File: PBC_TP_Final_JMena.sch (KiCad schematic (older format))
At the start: 0 parts

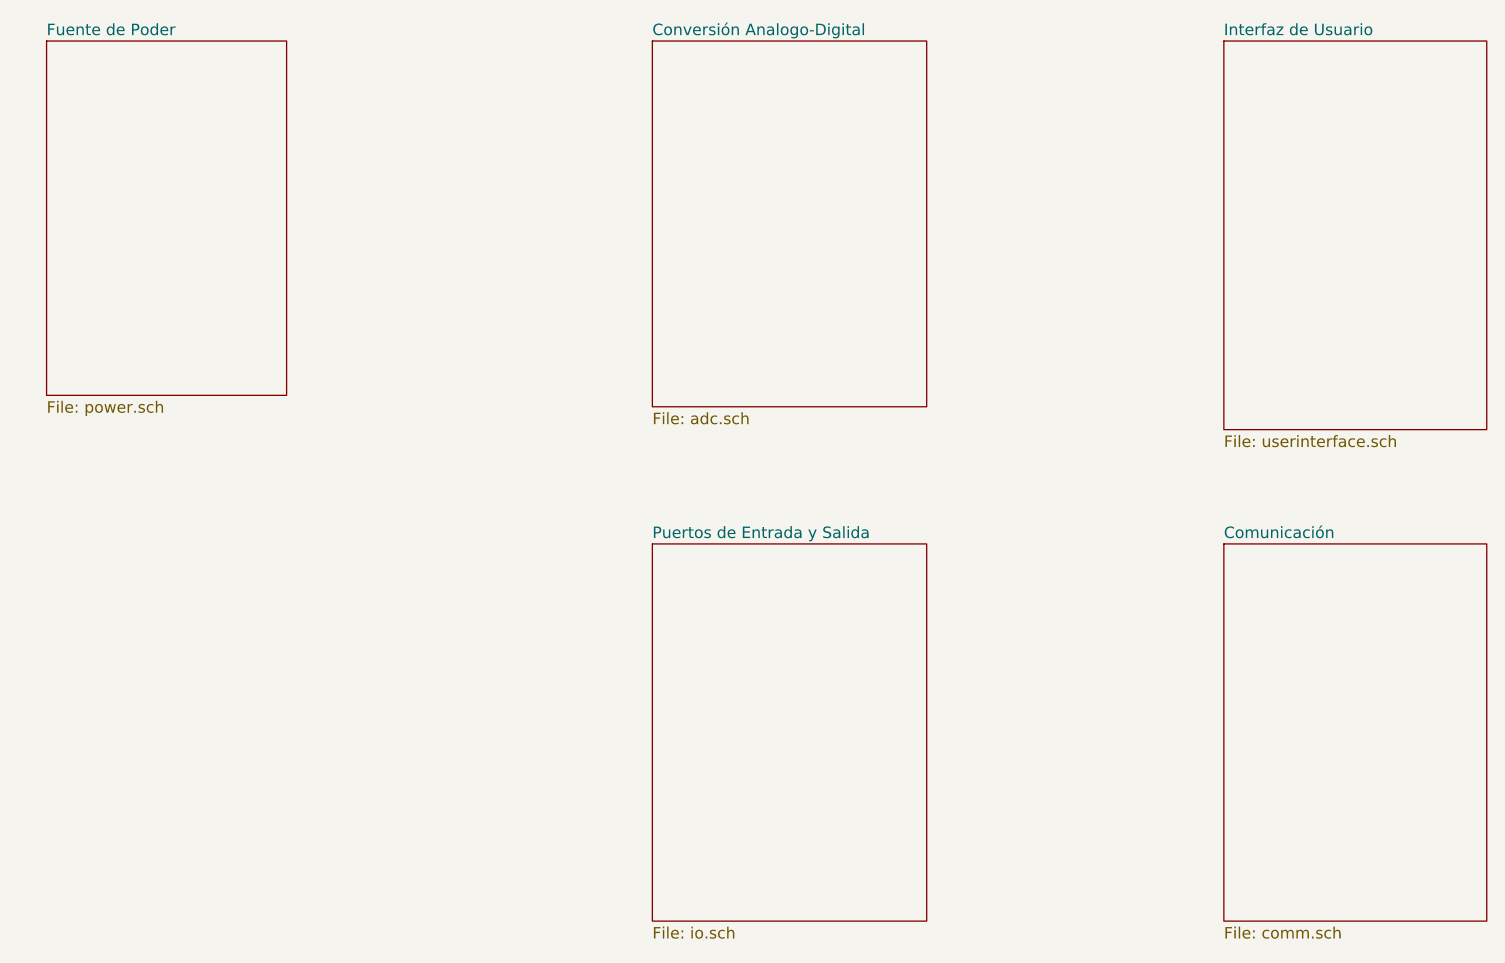
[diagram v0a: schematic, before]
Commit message: Se hace cambios en el esquematico y se anexa PCB
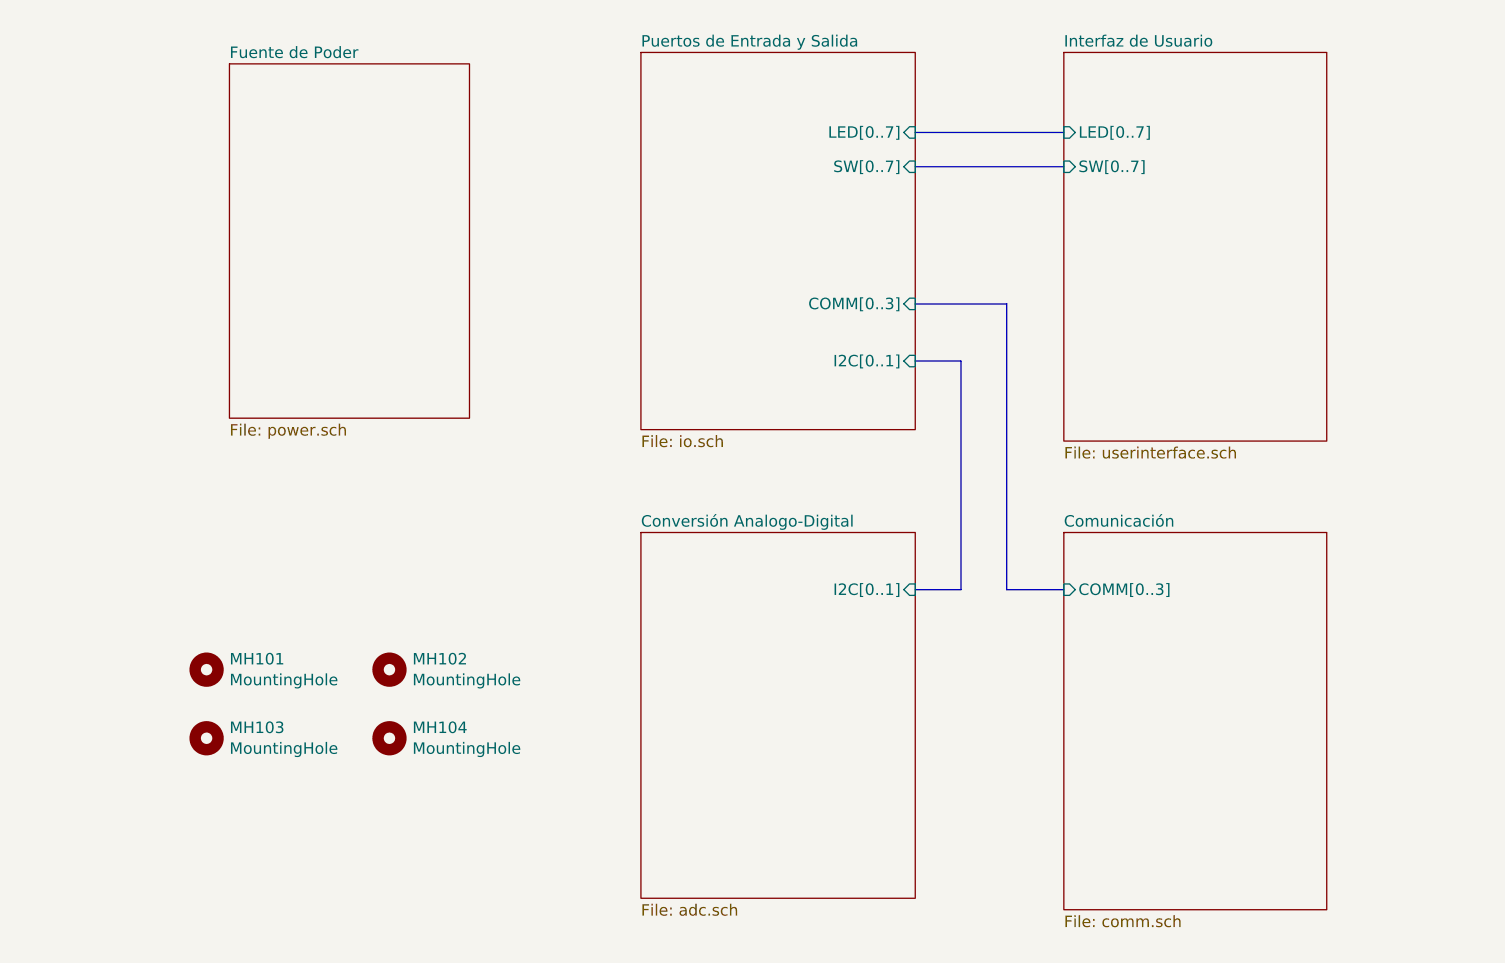
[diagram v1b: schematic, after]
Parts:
- added MH101, MH102, MH103, MH104: MountingHole, MountingHole:MountingHole_2.5mm, symbol Mechanical:MountingHole
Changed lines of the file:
@@
 $EndDescr
 $Sheet
-S 2750 1300 1050 1550
+S 3550 1400 1050 1550
 U 5BA8FAE3
 F0 "Fuente de Poder" 50
@@
 $EndSheet
 $Sheet
-S 5400 1300 1200 1600
+S 5350 3450 1200 1600
 U 5BA8FB15
 F0 "Conversión Analogo-Digital" 50
 F1 "adc.sch" 50
+F2 "I2C[0..1]" I R 6550 3700 50
 $EndSheet
+$Comp
+L Mechanical:MountingHole MH101
+U 1 1 5BB0B7F0
+P 3450 4050
+F 0 "MH101" H 3550 4096 50  0000 L CNN
+F 1 "MountingHole" H 3550 4005 50  0000 L CNN
+F 2 "MountingHole:MountingHole_2.5mm" H 3450 4050 50  0001 C CNN
+F 3 "~" H 3450 4050 50  0001 C CNN
+	1    3450 4050
+	1    0    0    -1
+$EndComp
+$Comp
+L Mechanical:MountingHole MH102
+U 1 1 5BB0B901
+P 4250 4050
+F 0 "MH102" H 4350 4096 50  0000 L CNN
+F 1 "MountingHole" H 4350 4005 50  0000 L CNN
+F 2 "MountingHole:MountingHole_2.5mm" H 4250 4050 50  0001 C CNN
+F 3 "~" H 4250 4050 50  0001 C CNN
+	1    4250 4050
+	1    0    0    -1
+$EndComp
+$Comp
+L Mechanical:MountingHole MH103
+U 1 1 5BB0B93D
+P 3450 4350
+F 0 "MH103" H 3550 4396 50  0000 L CNN
+F 1 "MountingHole" H 3550 4305 50  0000 L CNN
+F 2 "MountingHole:MountingHole_2.5mm" H 3450 4350 50  0001 C CNN
+F 3 "~" H 3450 4350 50  0001 C CNN
+	1    3450 4350
+	1    0    0    -1
+$EndComp
+$Comp
+L Mechanical:MountingHole MH104
+U 1 1 5BB0B985
+P 4250 4350
+F 0 "MH104" H 4350 4396 50  0000 L CNN
+F 1 "MountingHole" H 4350 4305 50  0000 L CNN
+F 2 "MountingHole:MountingHole_2.5mm" H 4250 4350 50  0001 C CNN
+F 3 "~" H 4250 4350 50  0001 C CNN
+	1    4250 4350
+	1    0    0    -1
+$EndComp
 $Sheet
-S 7900 1300 1150 1700
+S 7200 1350 1150 1700
 U 5BA8FB5C
 F0 "Interfaz de Usuario" 50
 F1 "userinterface.sch" 50
+F2 "LED[0..7]" I L 7200 1700 50
+F3 "SW[0..7]" I L 7200 1850 50
 $EndSheet
 $Sheet
-S 5400 3500 1200 1650
+S 5350 1350 1200 1650
 U 5BA8FCC3
 F0 "Puertos de Entrada y Salida" 50
 F1 "io.sch" 50
+F2 "LED[0..7]" I R 6550 1700 50
+F3 "SW[0..7]" I R 6550 1850 50
+F4 "COMM[0..3]" I R 6550 2450 50
+F5 "I2C[0..1]" I R 6550 2700 50
 $EndSheet
+Wire Bus Line
+	6550 1700 7200 1700
+Wire Bus Line
+	6550 1850 7200 1850
+Wire Bus Line
+	6550 2700 6750 2700
+Wire Bus Line
+	6750 2700 6750 3700
+Wire Bus Line
+	6750 3700 6550 3700
 $Sheet
-S 7900 3500 1150 1650
+S 7200 3450 1150 1650
 U 5BA8FCF6
 F0 "Comunicación" 50
 F1 "comm.sch" 50
+F2 "COMM[0..3]" I L 7200 3700 50
 $EndSheet
+Wire Bus Line
+	6950 2450 6550 2450
+Wire Bus Line
+	7200 3700 6950 3700
+Wire Bus Line
+	6950 3700 6950 2450
 $EndSCHEMATC

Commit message: Se realizan correcciones finales y se agregan carpetas BOM, Datasheet, Doc, Gerbers, lib.pretty y shapes3D
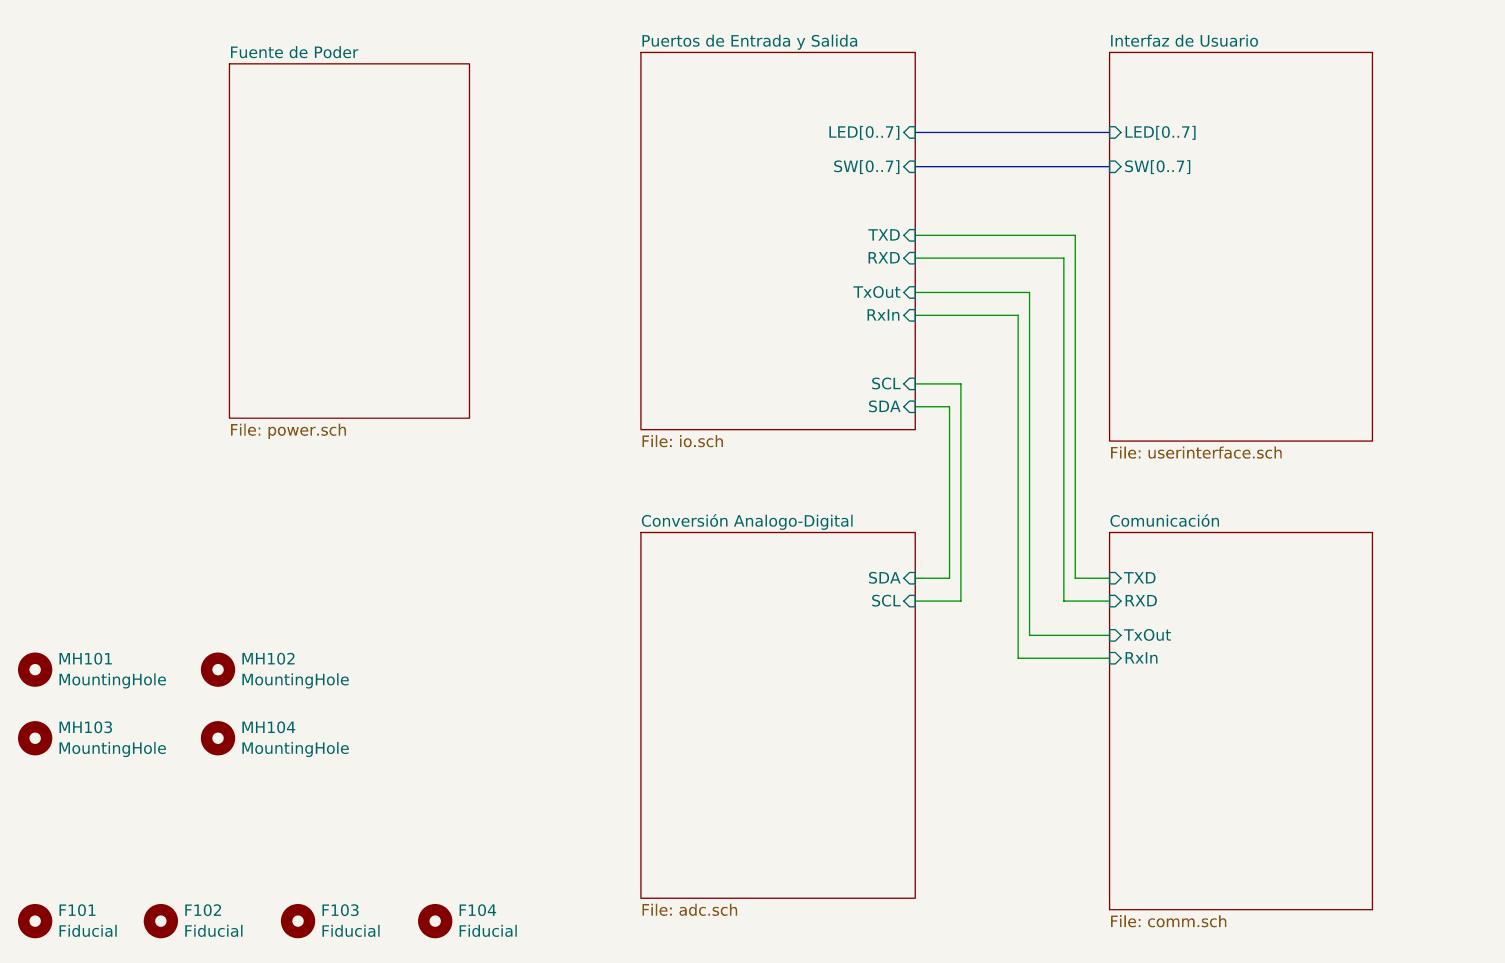
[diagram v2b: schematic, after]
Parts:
- added F101, F102, F103, F104: Fiducial, Fiducial:Fiducial_0.75mm_Dia_1.5mm_Outer, symbol Mechanical:MountingHole
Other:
- moved on the sheet: MH101, MH102, MH103, MH104
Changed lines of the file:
@@
 Sheet 1 6
 Title "PBC TP Final - Tarjeta de Expanción GEO-HCAL "
-Date "14/06/18"
+Date "2018-11-13"
 Rev "RG 1.0"
 Comp "GEO Technologies"
-Comment1 "Autor: Jairo Mena"
-Comment2 "Versión: 1.0"
-Comment3 ""
+Comment1 "Revisor: Telmo Moya"
+Comment2 "Autor: Jairo Mena"
+Comment3 "Versión: 1.0"
 Comment4 ""
 $EndDescr
@@
 F0 "Conversión Analogo-Digital" 50
 F1 "adc.sch" 50
-F2 "I2C[0..1]" I R 6550 3700 50
+F2 "SCL" I R 6550 3750 50
+F3 "SDA" I R 6550 3650 50
 $EndSheet
 $Comp
 L Mechanical:MountingHole MH101
 U 1 1 5BB0B7F0
-P 3450 4050
-F 0 "MH101" H 3550 4096 50  0000 L CNN
-F 1 "MountingHole" H 3550 4005 50  0000 L CNN
-F 2 "MountingHole:MountingHole_2.5mm" H 3450 4050 50  0001 C CNN
-F 3 "~" H 3450 4050 50  0001 C CNN
-	1    3450 4050
+P 2700 4050
+F 0 "MH101" H 2800 4096 50  0000 L CNN
+F 1 "MountingHole" H 2800 4005 50  0000 L CNN
+F 2 "MountingHole:MountingHole_2.5mm" H 2700 4050 50  0001 C CNN
+F 3 "~" H 2700 4050 50  0001 C CNN
+	1    2700 4050
 	1    0    0    -1
 $EndComp
@@
 L Mechanical:MountingHole MH102
 U 1 1 5BB0B901
-P 4250 4050
-F 0 "MH102" H 4350 4096 50  0000 L CNN
-F 1 "MountingHole" H 4350 4005 50  0000 L CNN
-F 2 "MountingHole:MountingHole_2.5mm" H 4250 4050 50  0001 C CNN
-F 3 "~" H 4250 4050 50  0001 C CNN
-	1    4250 4050
+P 3500 4050
+F 0 "MH102" H 3600 4096 50  0000 L CNN
+F 1 "MountingHole" H 3600 4005 50  0000 L CNN
+F 2 "MountingHole:MountingHole_2.5mm" H 3500 4050 50  0001 C CNN
+F 3 "~" H 3500 4050 50  0001 C CNN
+	1    3500 4050
 	1    0    0    -1
 $EndComp
@@
 L Mechanical:MountingHole MH103
 U 1 1 5BB0B93D
-P 3450 4350
-F 0 "MH103" H 3550 4396 50  0000 L CNN
-F 1 "MountingHole" H 3550 4305 50  0000 L CNN
-F 2 "MountingHole:MountingHole_2.5mm" H 3450 4350 50  0001 C CNN
-F 3 "~" H 3450 4350 50  0001 C CNN
-	1    3450 4350
+P 2700 4350
+F 0 "MH103" H 2800 4396 50  0000 L CNN
+F 1 "MountingHole" H 2800 4305 50  0000 L CNN
+F 2 "MountingHole:MountingHole_2.5mm" H 2700 4350 50  0001 C CNN
+F 3 "~" H 2700 4350 50  0001 C CNN
+	1    2700 4350
 	1    0    0    -1
 $EndComp
@@
 L Mechanical:MountingHole MH104
 U 1 1 5BB0B985
-P 4250 4350
-F 0 "MH104" H 4350 4396 50  0000 L CNN
-F 1 "MountingHole" H 4350 4305 50  0000 L CNN
-F 2 "MountingHole:MountingHole_2.5mm" H 4250 4350 50  0001 C CNN
-F 3 "~" H 4250 4350 50  0001 C CNN
-	1    4250 4350
+P 3500 4350
+F 0 "MH104" H 3600 4396 50  0000 L CNN
+F 1 "MountingHole" H 3600 4305 50  0000 L CNN
+F 2 "MountingHole:MountingHole_2.5mm" H 3500 4350 50  0001 C CNN
+F 3 "~" H 3500 4350 50  0001 C CNN
+	1    3500 4350
 	1    0    0    -1
 $EndComp
 $Sheet
-S 7200 1350 1150 1700
+S 7400 1350 1150 1700
 U 5BA8FB5C
 F0 "Interfaz de Usuario" 50
 F1 "userinterface.sch" 50
-F2 "LED[0..7]" I L 7200 1700 50
-F3 "SW[0..7]" I L 7200 1850 50
+F2 "LED[0..7]" I L 7400 1700 50
+F3 "SW[0..7]" I L 7400 1850 50
+$EndSheet
+$Sheet
+S 7400 3450 1150 1650
+U 5BA8FCF6
+F0 "Comunicación" 50
+F1 "comm.sch" 50
+F2 "RxIn" I L 7400 4000 50
+F3 "TxOut" I L 7400 3900 50
+F4 "TXD" I L 7400 3650 50
+F5 "RXD" I L 7400 3750 50
 $EndSheet
 $Sheet
@@
 F2 "LED[0..7]" I R 6550 1700 50
 F3 "SW[0..7]" I R 6550 1850 50
-F4 "COMM[0..3]" I R 6550 2450 50
-F5 "I2C[0..1]" I R 6550 2700 50
+F4 "SCL" I R 6550 2800 50
+F5 "SDA" I R 6550 2900 50
+F6 "TXD" I R 6550 2150 50
+F7 "RXD" I R 6550 2250 50
+F8 "RxIn" I R 6550 2500 50
+F9 "TxOut" I R 6550 2400 50
 $EndSheet
+Wire Wire Line
+	6550 2900 6700 2900
+Wire Wire Line
+	6700 2900 6700 3650
+Wire Wire Line
+	6700 3650 6550 3650
+Wire Wire Line
+	6550 3750 6750 3750
+Wire Wire Line
+	6750 3750 6750 2800
+Wire Wire Line
+	6750 2800 6550 2800
 Wire Bus Line
-	6550 1700 7200 1700
+	6550 1700 7400 1700
 Wire Bus Line
-	6550 1850 7200 1850
-Wire Bus Line
-	6550 2700 6750 2700
-Wire Bus Line
-	6750 2700 6750 3700
-Wire Bus Line
-	6750 3700 6550 3700
-$Sheet
-S 7200 3450 1150 1650
-U 5BA8FCF6
-F0 "Comunicación" 50
-F1 "comm.sch" 50
-F2 "COMM[0..3]" I L 7200 3700 50
-$EndSheet
-Wire Bus Line
-	6950 2450 6550 2450
-Wire Bus Line
-	7200 3700 6950 3700
-Wire Bus Line
-	6950 3700 6950 2450
+	6550 1850 7400 1850
+Wire Wire Line
+	7400 4000 7000 4000
+Wire Wire Line
+	7000 4000 7000 2500
+Wire Wire Line
+	7000 2500 6550 2500
+Wire Wire Line
+	7400 3900 7050 3900
+Wire Wire Line
+	7050 3900 7050 2400
+Wire Wire Line
+	7050 2400 6550 2400
+Wire Wire Line
+	6550 2250 7200 2250
+Wire Wire Line
+	7200 2250 7200 3750
+Wire Wire Line
+	7200 3750 7400 3750
+Wire Wire Line
+	7400 3650 7250 3650
+Wire Wire Line
+	7250 3650 7250 2150
+Wire Wire Line
+	7250 2150 6550 2150
+$Comp
+L Mechanical:MountingHole F101
+U 1 1 5BEC591E
+P 2700 5150
+F 0 "F101" H 2800 5196 50  0000 L CNN
+F 1 "Fiducial" H 2800 5105 50  0000 L CNN
+F 2 "Fiducial:Fiducial_0.75mm_Dia_1.5mm_Outer" H 2700 5150 50  0001 C CNN
+F 3 "~" H 2700 5150 50  0001 C CNN
+	1    2700 5150
+	1    0    0    -1
+$EndComp
+$Comp
+L Mechanical:MountingHole F102
+U 1 1 5BEC59DD
+P 3250 5150
+F 0 "F102" H 3350 5196 50  0000 L CNN
+F 1 "Fiducial" H 3350 5105 50  0000 L CNN
+F 2 "Fiducial:Fiducial_0.75mm_Dia_1.5mm_Outer" H 3250 5150 50  0001 C CNN
+F 3 "~" H 3250 5150 50  0001 C CNN
+	1    3250 5150
+	1    0    0    -1
+$EndComp
+$Comp
+L Mechanical:MountingHole F103
+U 1 1 5BEC73E0
+P 3850 5150
+F 0 "F103" H 3950 5196 50  0000 L CNN
+F 1 "Fiducial" H 3950 5105 50  0000 L CNN
+F 2 "Fiducial:Fiducial_0.75mm_Dia_1.5mm_Outer" H 3850 5150 50  0001 C CNN
+F 3 "~" H 3850 5150 50  0001 C CNN
+	1    3850 5150
+	1    0    0    -1
+$EndComp
+$Comp
+L Mechanical:MountingHole F104
+U 1 1 5BEC7412
+P 4450 5150
+F 0 "F104" H 4550 5196 50  0000 L CNN
+F 1 "Fiducial" H 4550 5105 50  0000 L CNN
+F 2 "Fiducial:Fiducial_0.75mm_Dia_1.5mm_Outer" H 4450 5150 50  0001 C CNN
+F 3 "~" H 4450 5150 50  0001 C CNN
+	1    4450 5150
+	1    0    0    -1
+$EndComp
 $EndSCHEMATC
